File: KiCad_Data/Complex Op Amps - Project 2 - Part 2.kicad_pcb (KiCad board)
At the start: 2 copper layers, 184.2 x 82.1 mm, 124 parts, among them P1 Potentiometer P/N: 3590P-2-**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, P2 Potentiometer P/N: 3590P-2-**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, SW1 SPDT Switch, P/N: 7101SD9AV2BE, SW2 SPDT Switch, P/N: 7101SD9AV2BE, SW3 SPDT Switch, P/N: 7101SD9AV2BE, SW4 SPDT Switch, P/N: 7101SD9AV2BE, SW5 SPDT Switch, P/N: 7101SD9AV2BE, SW6 SPDT Switch, P/N: 7101SD9AV2BE, SW7 SPDT Switch, P/N: 7101SD9AV2BE, T1 Transistor P/N: 2N3906, T2 Transistor P/N: 2N3906, T3 Transistor P/N: 2N3906, T4 Transistor P/N: 2N3906

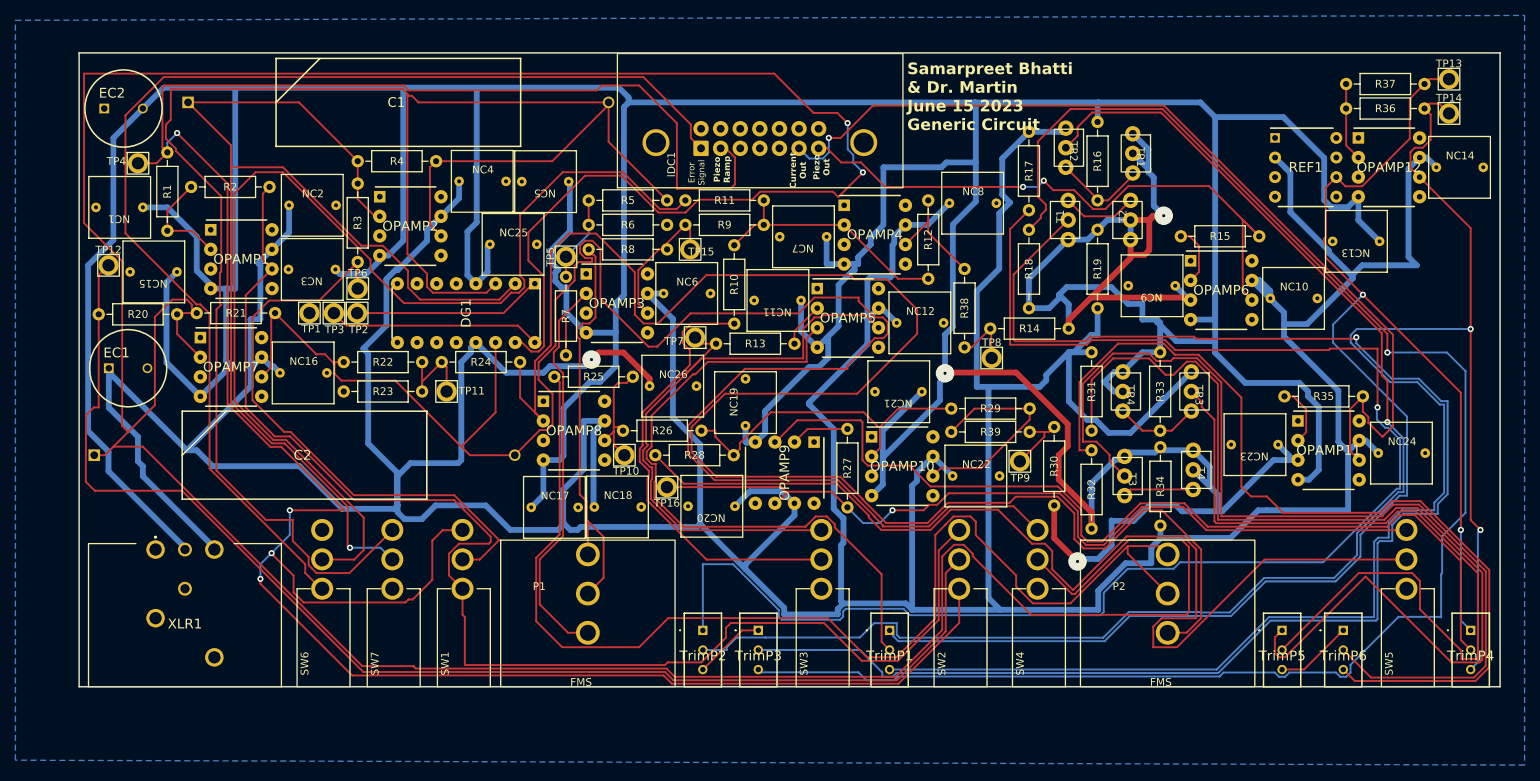
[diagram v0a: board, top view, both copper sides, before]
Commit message: Changed Names
Naming was updated for the symbols to make more sense (adding values for resistance, what each switch does, etc)
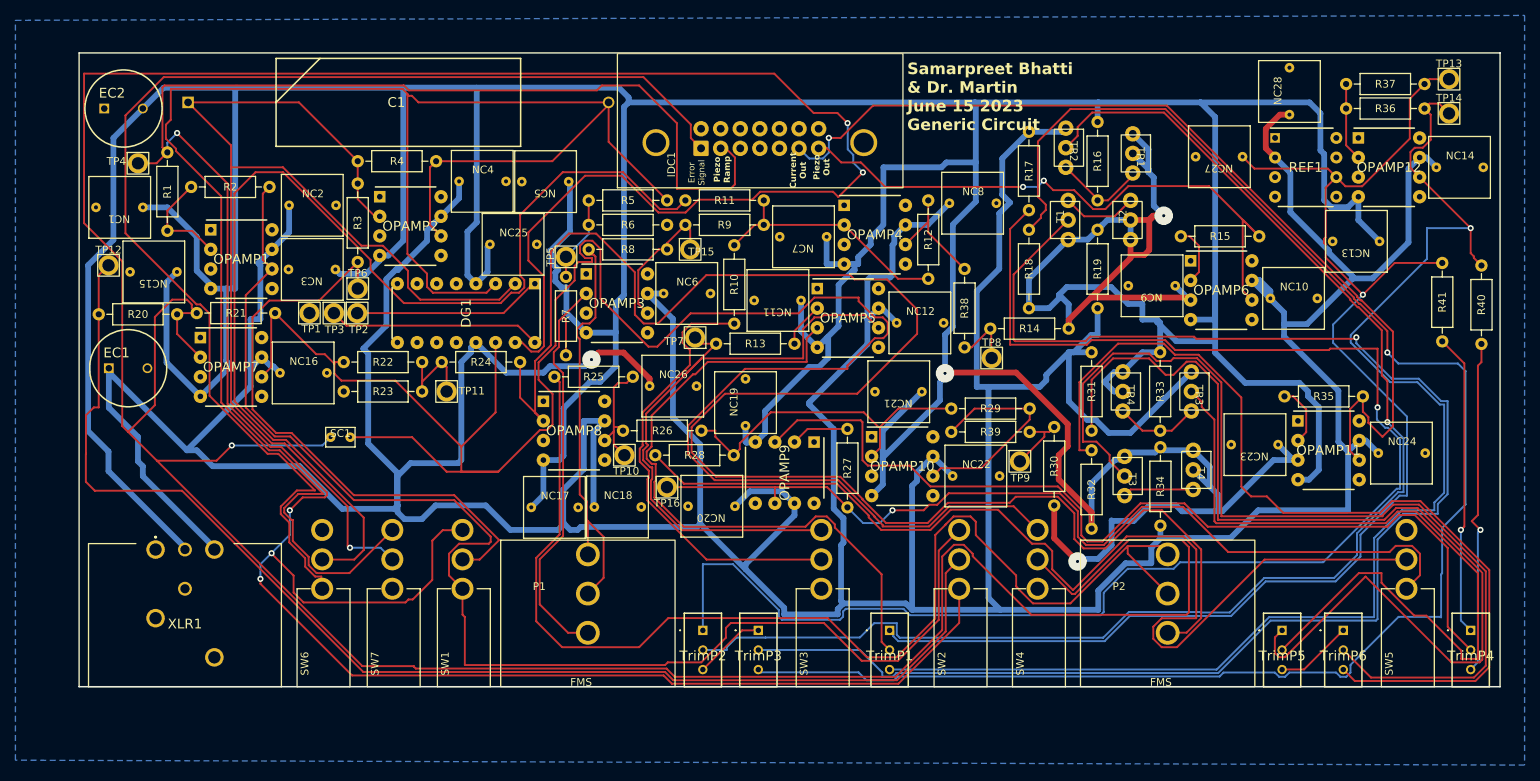
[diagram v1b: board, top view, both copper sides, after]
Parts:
- removed C2: ~, Complex_Op_Amps_Footprints:Polypropylene Capacitor
- added NC27: 0.1uF, Complex_Op_Amps_Footprints:CAPACITOR - 399-4209-ND, F.Cu at (171.8, 86.6)
- added NC28: 0.1uF, Complex_Op_Amps_Footprints:CAPACITOR - 399-4209-ND, F.Cu at (180.0, 77.1)
- added R40: 20k, Complex_Op_Amps_Footprints:R_Axial_DIN0207_L6.3mm_D2.5mm_P10.16mm_Horizontal, F.Cu at (205.9, 99.7)
- added R41: 20k, Complex_Op_Amps_Footprints:R_Axial_DIN0207_L6.3mm_D2.5mm_P10.16mm_Horizontal, F.Cu at (200.8, 109.6)
- added SC1: 1nF, Complex_Op_Amps_Footprints:Small Capacitor, F.Cu at (58.0, 122.0)
- C1: value ~ -> 1uF
- EC1, EC2: value P/N: EEU-EB1C102 -> 1000uF
- NC1, NC10, NC11, NC12, NC13, NC14, NC15, NC16, NC17, NC18, NC19, NC2, NC20, NC21, NC22, NC23, NC24, NC25, NC26, NC3, NC4, NC5, NC6, NC7, NC8, NC9: value Normal_Capacitor, P/N: 399-4209-ND -> 0.1uF
- P1, P2: value Potentiometer P/N: 3590P-2-***L -> 50k
- R1, R10, R11, R12, R14, R16, R19, R2, R20, R21, R26, R28, R29, R3, R33, R34, R36, R37, R4, R8, R9: value Generic Resistor -> 10k
- R13, R15, R24, R25, R27, R35, R7: value Generic Resistor -> 1k
- R17, R18: value Generic Resistor -> 5k
- R22, R38, R39, R5: value Generic Resistor -> 0k
- R23, R6: value Generic Resistor -> Open
- R30, R31, R32: value Generic Resistor -> 20k
- TrimP1: value P/N: 3296X-1-**** -> 20k
- TrimP2, TrimP3, TrimP4: value P/N: 3296X-1-**** -> 10k
- TrimP5, TrimP6: value P/N: 3296X-1-**** -> 5k
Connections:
- OPAMP1 pad 8: (no net) -> unconnected-(OPAMP1-NC-Pad8)
- OPAMP10 pad 8: (no net) -> unconnected-(OPAMP10-NC-Pad8)
- OPAMP11 pad 8: (no net) -> unconnected-(OPAMP11-NC-Pad8)
- OPAMP12 pad 8: (no net) -> unconnected-(OPAMP12-NC-Pad8)
- OPAMP2 pad 8: (no net) -> unconnected-(OPAMP2-NC-Pad8)
- OPAMP3 pad 8: (no net) -> unconnected-(OPAMP3-NC-Pad8)
- OPAMP4 pad 8: (no net) -> unconnected-(OPAMP4-NC-Pad8)
- OPAMP5 pad 8: (no net) -> unconnected-(OPAMP5-NC-Pad8)
- OPAMP6 pad 8: (no net) -> unconnected-(OPAMP6-NC-Pad8)
- OPAMP7 pad 8: (no net) -> unconnected-(OPAMP7-NC-Pad8)
- OPAMP8 pad 8: (no net) -> unconnected-(OPAMP8-NC-Pad8)
- OPAMP9 pad 6: Net-(SW5-C) -> Net-(SW5-A)
- OPAMP9 pad 8: (no net) -> unconnected-(OPAMP9-NC-Pad8)
- R27 pad 2: Net-(SW5-C) -> Net-(SW5-A)
- SW5 pad 1: GND -> Net-(SW5-A)
- SW5 pad 3: Net-(SW5-C) -> GND
- TP16 pad 1: Net-(SW5-C) -> Net-(SW5-A)
- TrimP4 pad 1: +5V -> Net-(R41-Pad1)
- TrimP4 pad 3: -5V -> Net-(R40-Pad2)
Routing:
- net Net-(SW5-A): track 0.00 -> 118.4 mm, vias 0 -> 1
- net Net-(SW5-C): track 109.7 -> 0.00 mm, vias 1 -> 0
- net -5V: track 215.4 -> 169.5 mm, vias 2 -> 1
- net Net-(R40-Pad2): track 0.00 -> 43.7 mm, vias 0 -> 1
- net Net-(R41-Pad1): track 0.00 -> 39.3 mm, vias 0 -> 1
- net Net-(DG1B-S2): track 241.6 -> 266.8 mm
- net +5V: track 199.8 -> 175.8 mm, vias 2 -> 1
- net Net-(DG1B-D2): track 468.5 -> 486.1 mm, vias 2 -> 3
- net Net-(SW6-A): track 153.7 -> 160.0 mm
- net -15V: track 931.9 -> 937.0 mm
- net +15V: track 771.4 -> 776.3 mm
- net Net-(DG1A-S1): track 230.7 -> 235.0 mm
- net Net-(SW1-C): track 322.6 -> 318.3 mm
- net Net-(TR3-B): track 104.3 -> 102.9 mm
- net Net-(T1-B): track 199.8 -> 198.8 mm
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
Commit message: Fixed Wiring that was close to edge
This version is our first ordered version
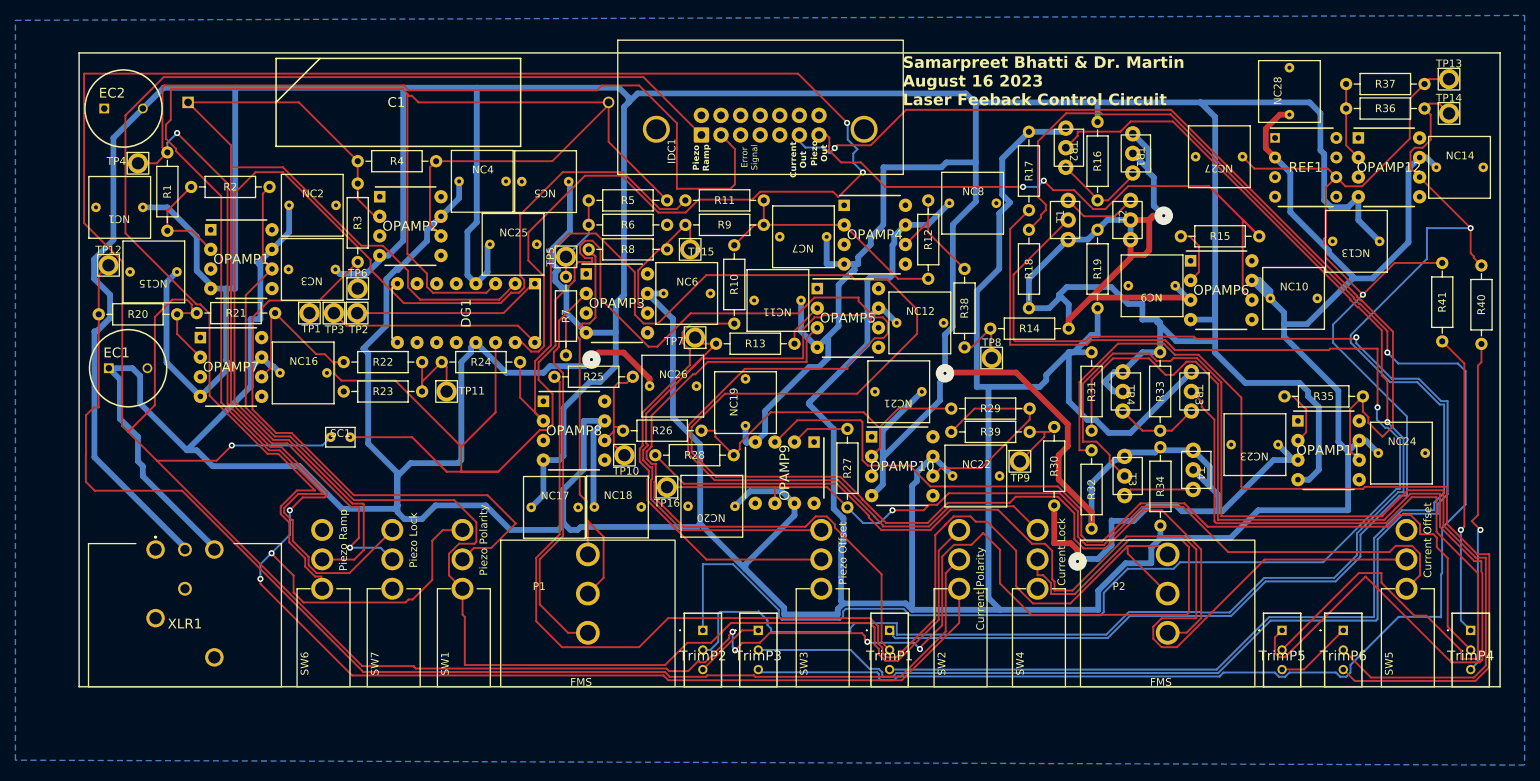
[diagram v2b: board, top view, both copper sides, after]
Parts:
- moved IDC1 1.73 mm to (93.9, 87.9)
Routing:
- net Net-(DG1B-D2): track 486.1 -> 497.0 mm, vias 3 -> 7
- net Net-(T3-B): track 125.4 -> 130.6 mm
- net Net-(R31-Pad2): track 133.5 -> 138.3 mm
- net Net-(SW1-B): track 76.7 -> 81.1 mm
- net Net-(TR3-B): track 102.9 -> 107.0 mm
- net Net-(TR2-B): track 181.0 -> 184.5 mm
- net -15V: track 937.0 -> 940.5 mm
- net Net-(R32-Pad1): track 118.7 -> 121.6 mm
- net Net-(P2-Pad2): track 152.4 -> 154.9 mm
- net Net-(DG1A-D1): track 154.0 -> 155.8 mm
- net +15V: track 776.3 -> 778.0 mm
- net Net-(SW6-A): track 160.0 -> 158.3 mm
- net Net-(IDC1-C-Pad7): track 78.9 -> 80.6 mm
- net Net-(SW1-A): track 172.9 -> 171.2 mm
- net Net-(SW1-C): track 318.3 -> 319.9 mm
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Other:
- board text added: "Samarpreet Bhatti & Dr. Martin August 16 2023 Laser Feeback Control Circuit"
- board text removed: "Samarpreet Bhatti & Dr. Martin June 15 2023 Generic Circuit"

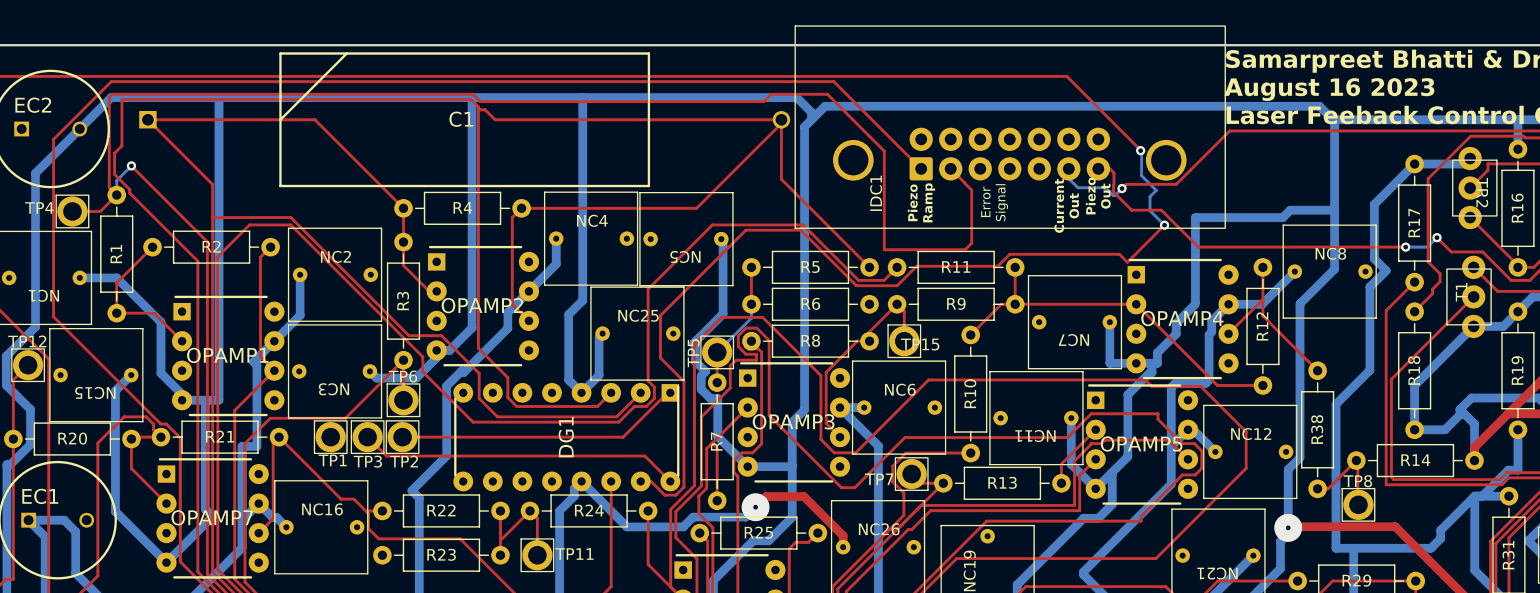
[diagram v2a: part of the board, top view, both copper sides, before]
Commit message: Updated IDC connections
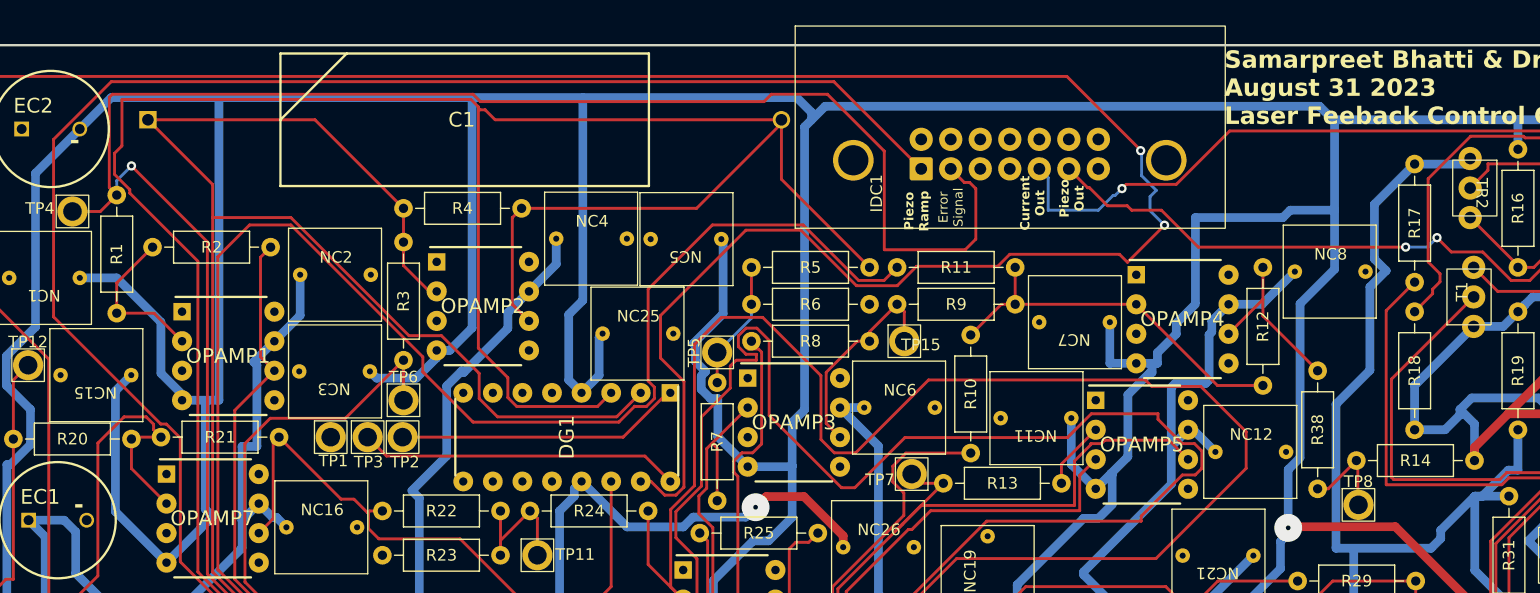
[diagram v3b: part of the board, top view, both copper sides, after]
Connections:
- IDC1 pad 5: GND -> Net-(IDC1-C-Pad5)
- IDC1 pad 7: Net-(IDC1-C-Pad7) -> GND
- OPAMP11 pad 6: Net-(IDC1-C-Pad6) -> Net-(IDC1-C-Pad5)
- OPAMP6 pad 6: Net-(IDC1-C-Pad7) -> Net-(IDC1-C-Pad6)
- R15 pad 2: Net-(IDC1-C-Pad7) -> Net-(IDC1-C-Pad6)
- R35 pad 2: Net-(IDC1-C-Pad6) -> Net-(IDC1-C-Pad5)
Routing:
- net Net-(IDC1-C-Pad5): track 0.00 -> 127.3 mm, vias 0 -> 1
- net Net-(IDC1-C-Pad7): track 80.6 -> 0.00 mm, vias 2 -> 0
- net Net-(IDC1-C-Pad6): track 122.6 -> 82.9 mm, vias 1 -> 2
- net Net-(SW1-C): track 319.9 -> 320.5 mm
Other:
- board text added: "-"
- board text added: "Samarpreet Bhatti & Dr. Martin August 31 2023 Laser Feeback Control Circuit"
- board text removed: "Samarpreet Bhatti & Dr. Martin August 16 2023 Laser Feeback Control Circuit"
